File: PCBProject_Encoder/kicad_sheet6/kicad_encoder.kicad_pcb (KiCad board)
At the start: 4 copper layers, 74.7 x 33.9 mm, 73 parts, among them J1 L77HDE15SD1CH4RHNVGA, J2 HIF3FC-10PA-2.54DSA, U1 DS3486M, U2 DS3486M, U3 SN74HC365D

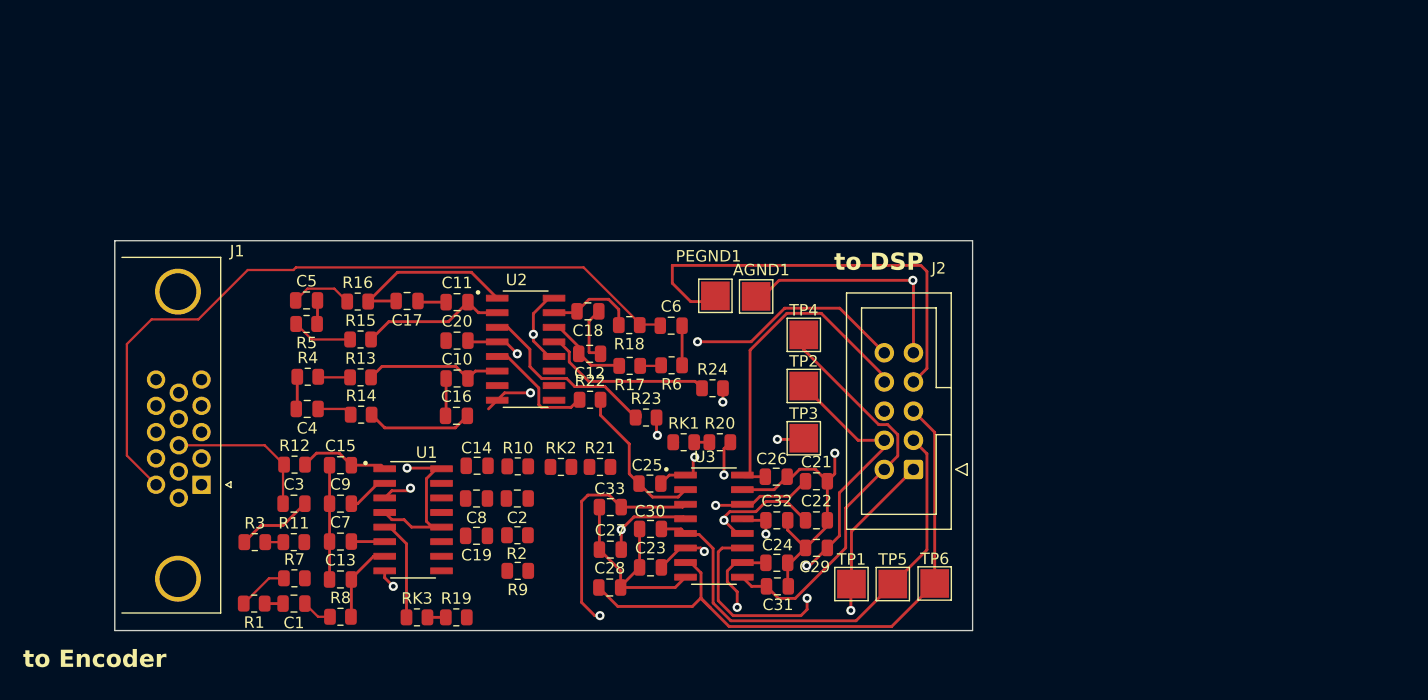
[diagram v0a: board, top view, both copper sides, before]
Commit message: 将编码器改为两层，文件为：kicad_encoder.kicad_pcb
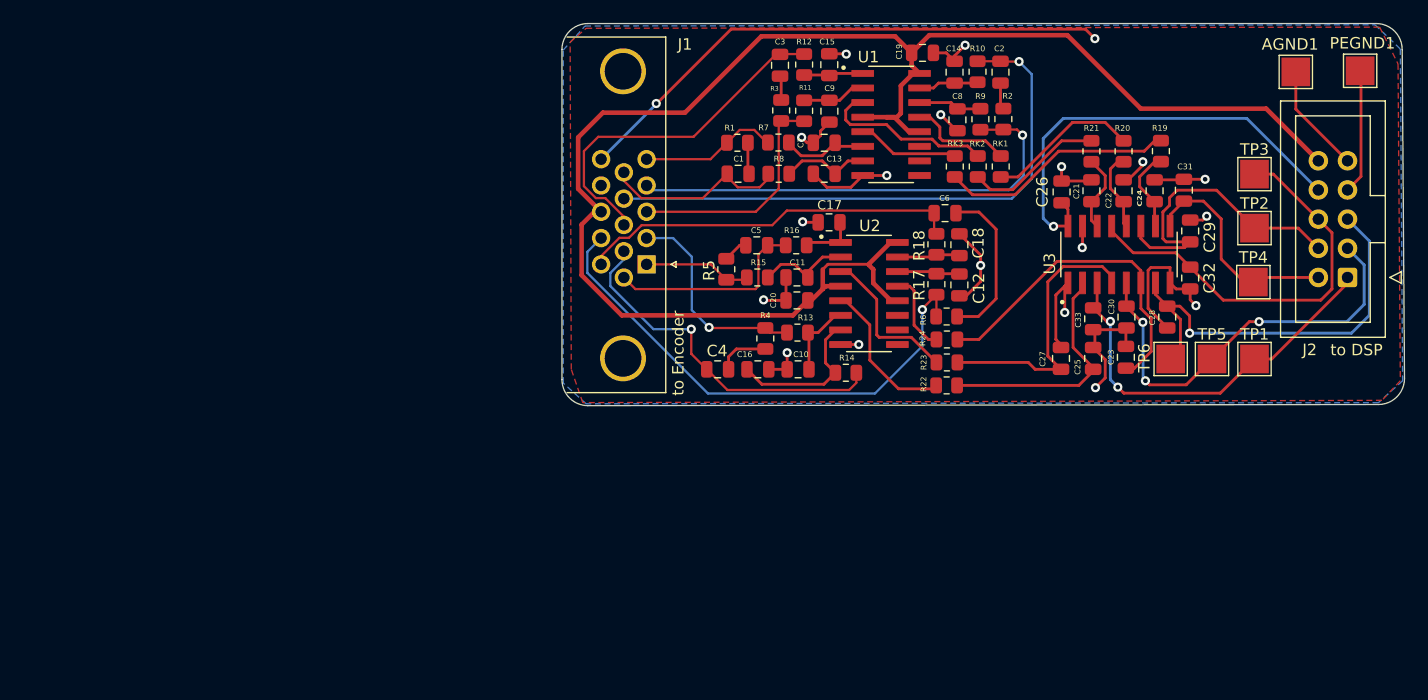
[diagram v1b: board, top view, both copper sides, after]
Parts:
- moved R19 73.6 mm to (149.8, 84.1), turned to -90 degrees
- moved RK3 61.1 mm to (131.8, 85.4), turned to -90 degrees
- moved PEGND1 59.5 mm to (167.1, 77.1)
- moved R3 59.3 mm to (116.7, 80.6), turned to -90 degrees
- moved R11 58.2 mm to (118.7, 80.6), turned to 90 degrees
- moved R1 58.1 mm to (112.9, 83.4)
- moved C19 57.3 mm to (129.0, 75.5)
- moved C3 57.0 mm to (116.6, 76.6), turned to -90 degrees
- moved R7 56.7 mm to (116.4, 83.3)
- moved R12 56.4 mm to (118.7, 76.6), turned to -90 degrees
- moved R9 56.3 mm to (134.0, 81.3), turned to 90 degrees
- moved C2 56.1 mm to (135.8, 77.2), turned to -90 degrees
- moved R2 55.7 mm to (136.0, 81.3), turned to -90 degrees
- moved C15 55.0 mm to (120.9, 76.6), turned to -90 degrees
- moved C13 55.0 mm to (120.4, 86.1)
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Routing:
- net AGND: track 160.3 -> 90.7 mm, vias 5 -> 18
- net D+5V: track 82.3 -> 141.7 mm, vias 4 -> 0
- net /ENCB-: track 0.00 -> 50.5 mm, vias 0 -> 1
- net /HALL_W+: track 1.85 -> 45.7 mm, vias 0 -> 1
- net /ENCB+: track 0.00 -> 41.1 mm, vias 0 -> 1
- net /HALL_W-: track 64.5 -> 33.4 mm
- net /HALL_U-: track 3.04 -> 31.5 mm, vias 0 -> 1
- net Net-(U3-4A): track 31.7 -> 6.71 mm, vias 1 -> 0
- net /QEP1_HALL_U: track 58.2 -> 35.0 mm
- net PE_GND: track 37.4 -> 59.0 mm, vias 0 -> 2
- net /ENCZ+: track 1.58 -> 20.3 mm
- net Net-(R19-Pad1): track 1.60 -> 20.3 mm
- net /ENCZ-: track 13.3 -> 31.0 mm
- net /QEP1_HALL_W: track 53.7 -> 37.1 mm, vias 0 -> 1
- net /MQEP1A: track 35.9 -> 19.5 mm
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- added copper zone on B.Cu, net AGND
- added copper zone on F.Cu, net PE_GND
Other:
- board size 74.7 x 33.9 mm -> 73.4 x 33.3 mm
- copper layers 4 -> 2
